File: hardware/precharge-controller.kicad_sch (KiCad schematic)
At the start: 0 parts

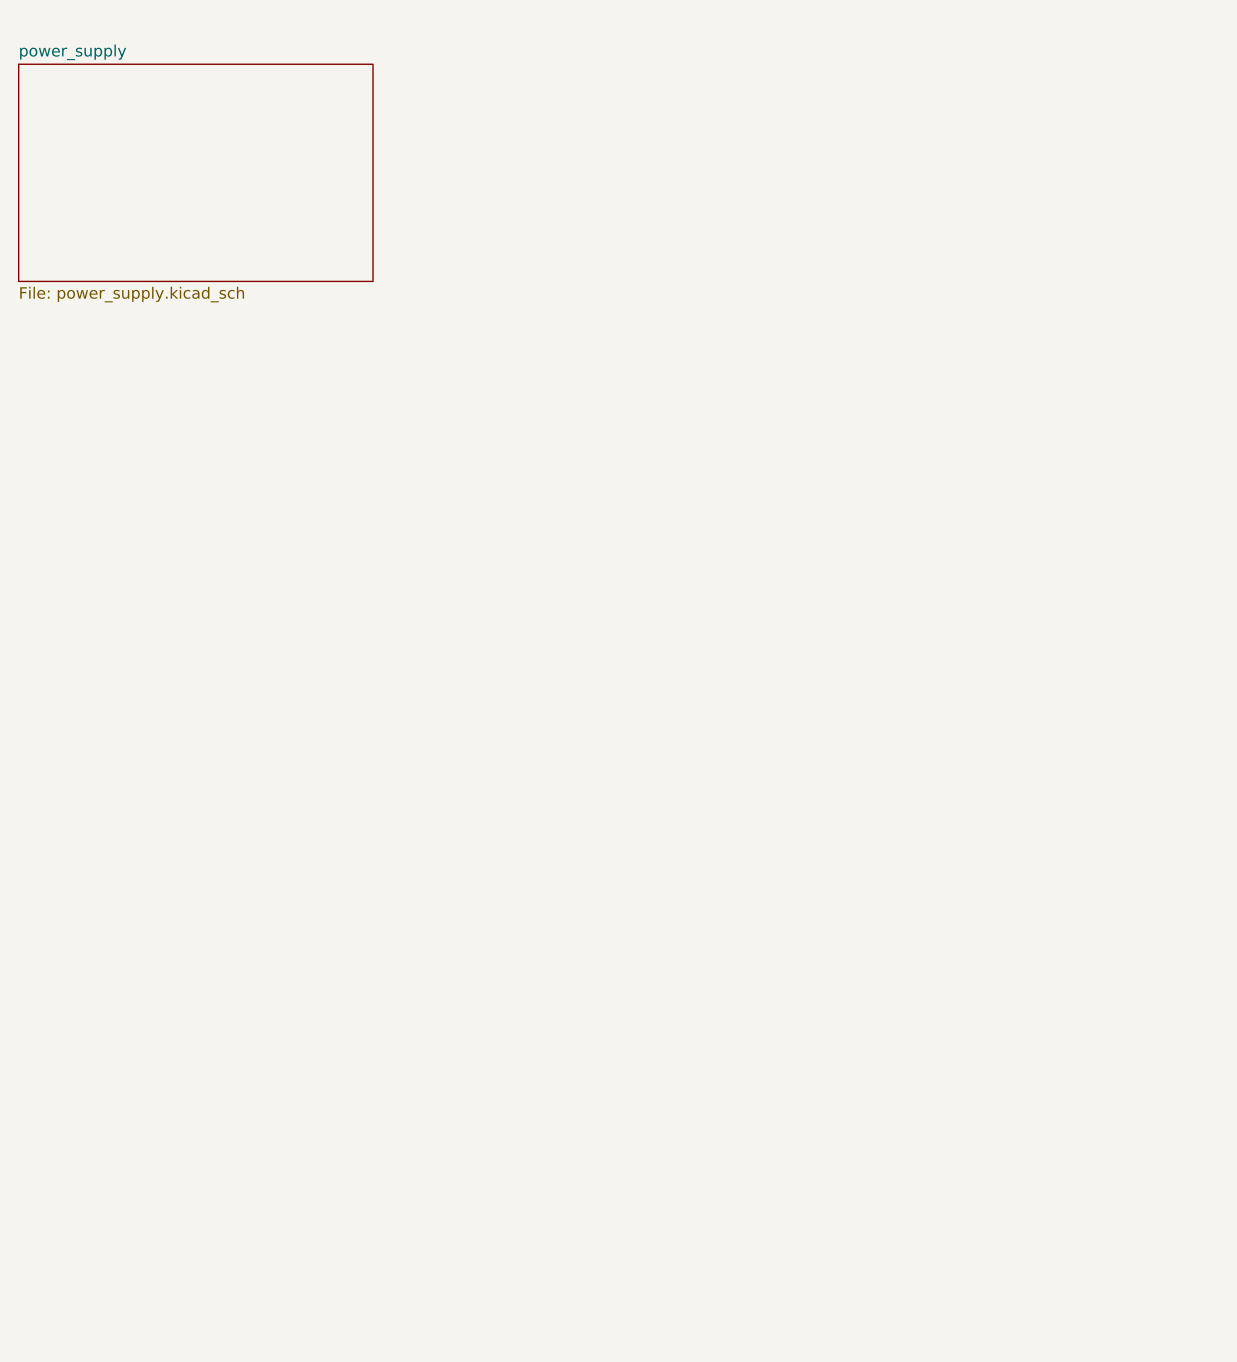
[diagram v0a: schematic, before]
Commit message: complete hierarchial sheet organization; start hv_sense schematic; start lv_logic schematic; refactor hierarchial sheets
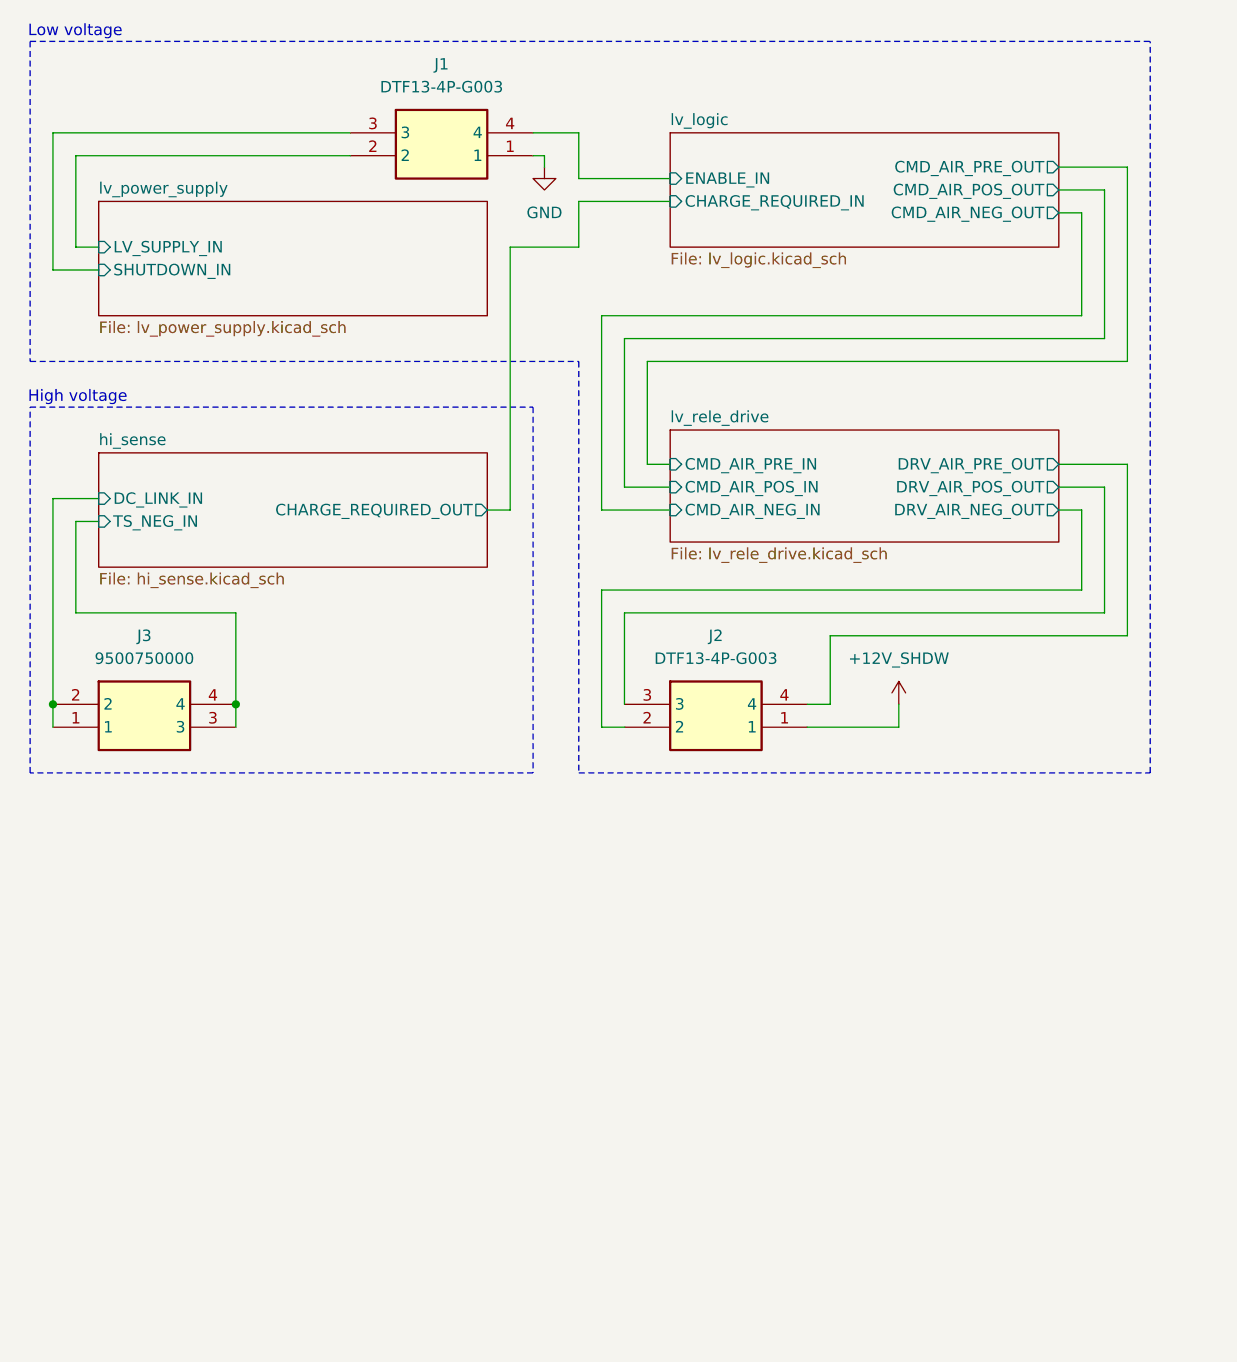
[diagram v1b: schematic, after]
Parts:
- added J1: DTF13-4P-G003, Library_Loader:DTF134PG003, symbol Libary_Loader:DTF13-4P-G003
- added J2: DTF13-4P-G003, DTF134PG003, symbol Libary_Loader:DTF13-4P-G003
- added J3: 9500750000, 9500750000, symbol Libary_Loader:9500750000
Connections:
- new net +12V_SHDW: J2.1
- new net GND: J1.1
- new net hi_sense/DC_LINK_IN: J3.1, J3.2
- new net hi_sense/TS_NEG_IN: J3.3, J3.4
- new net lv_logic/ENABLE_IN: J1.4
- new net lv_power_supply/LV_SUPPLY_IN: J1.2
- new net lv_power_supply/SHUTDOWN_IN: J1.3
- new net lv_rele_drive/DRV_AIR_NEG_OUT: J2.2
- new net lv_rele_drive/DRV_AIR_POS_OUT: J2.3
- new net lv_rele_drive/DRV_AIR_PRE_OUT: J2.4
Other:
- sheet power_supply renamed lv_power_supply
- added sheet hi_sense (hi_sense.kicad_sch)
- added sheet lv_logic (lv_logic.kicad_sch)
- added sheet lv_rele_drive (lv_rele_drive.kicad_sch)
- sheet lv_power_supply: file power_supply.kicad_sch -> lv_power_supply.kicad_sch
- sheet lv_power_supply ports: added LV_SUPPLY_IN, SHUTDOWN_IN; removed none
- note added: "High voltage"
- note added: "Low voltage"

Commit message: add enable timer sizing in logic block
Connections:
- net GND: no longer J1.1
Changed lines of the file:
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@@
-	(wire
-		(pts
-			(xy 81.28 38.1) (xy 82.55 38.1)
-		)
-		(stroke
-			(width 0)
-			(type default)
-		)
-	)
 	(wire
 		(pts

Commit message: create hv_power hierarchical sheet; rename hi_sense ad hv_sense to meet project standards
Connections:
- net GND: now also J1.1
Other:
- sheet hi_sense renamed hv_sense
- added sheet hv_power (hv_power.kicad_sch)
- sheet hv_sense: file hi_sense.kicad_sch -> hv_sense.kicad_sch
- note added: "On PCB"
- note added: "Outside PCB"
- moved on the sheet: J1, J2, J3

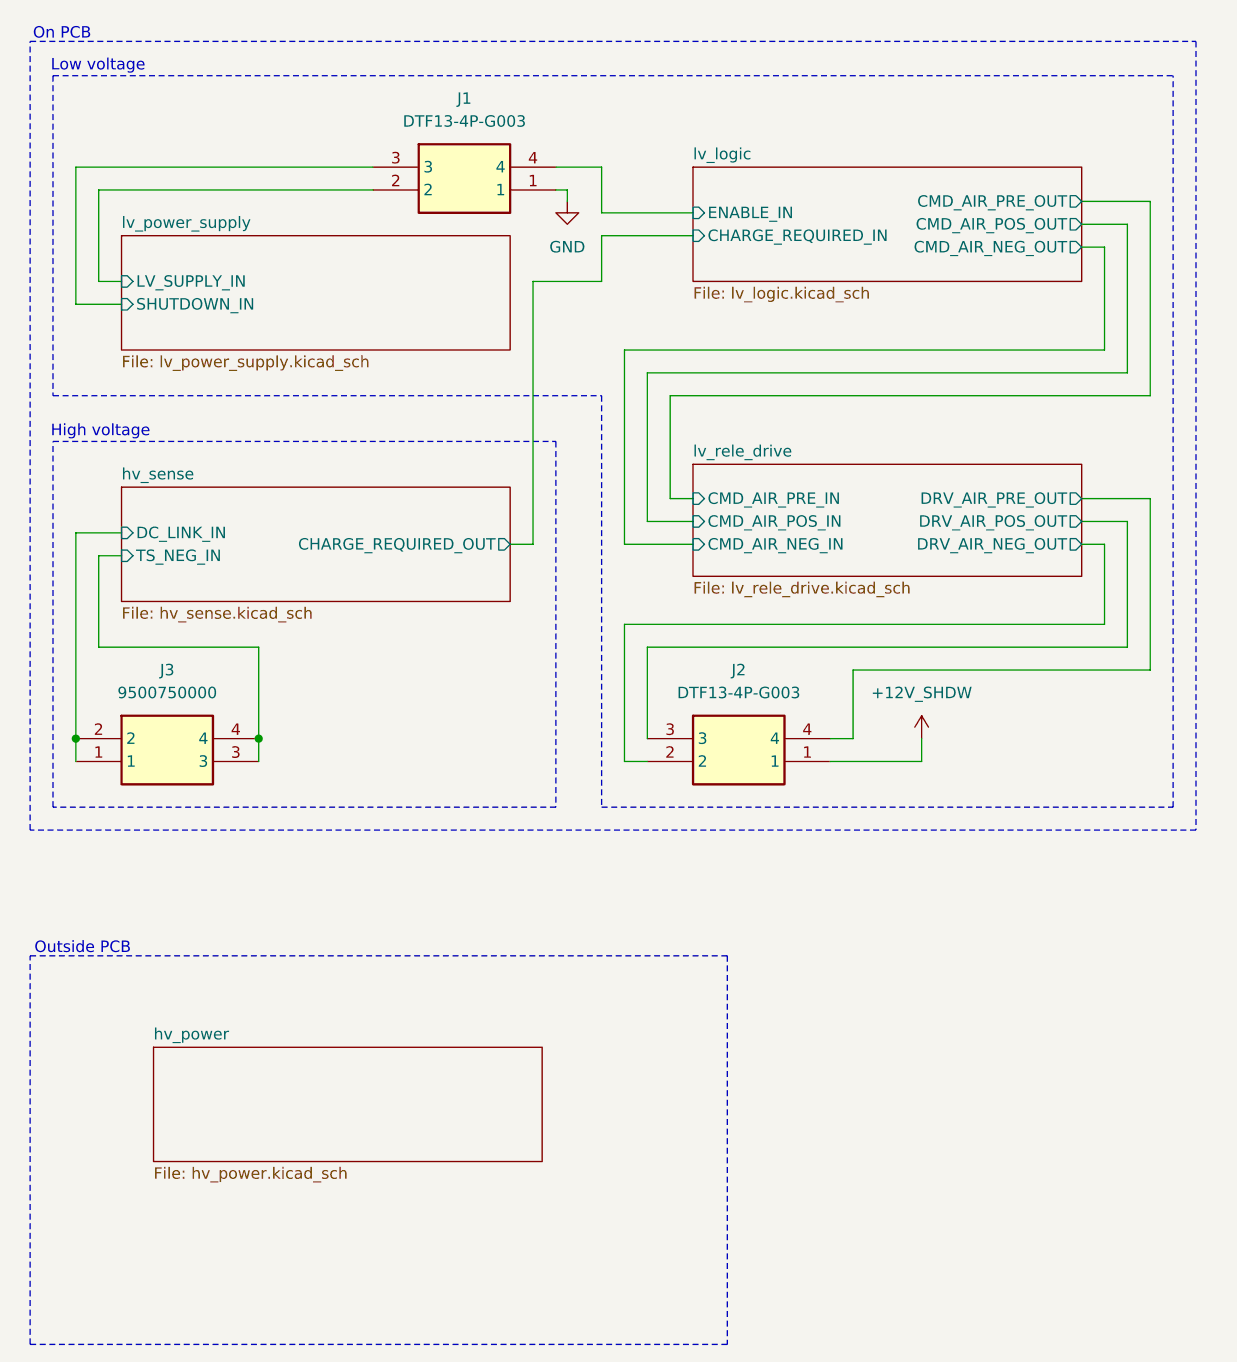
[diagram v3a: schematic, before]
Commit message: add traction system positive input to hv sense block with new dedicated connector
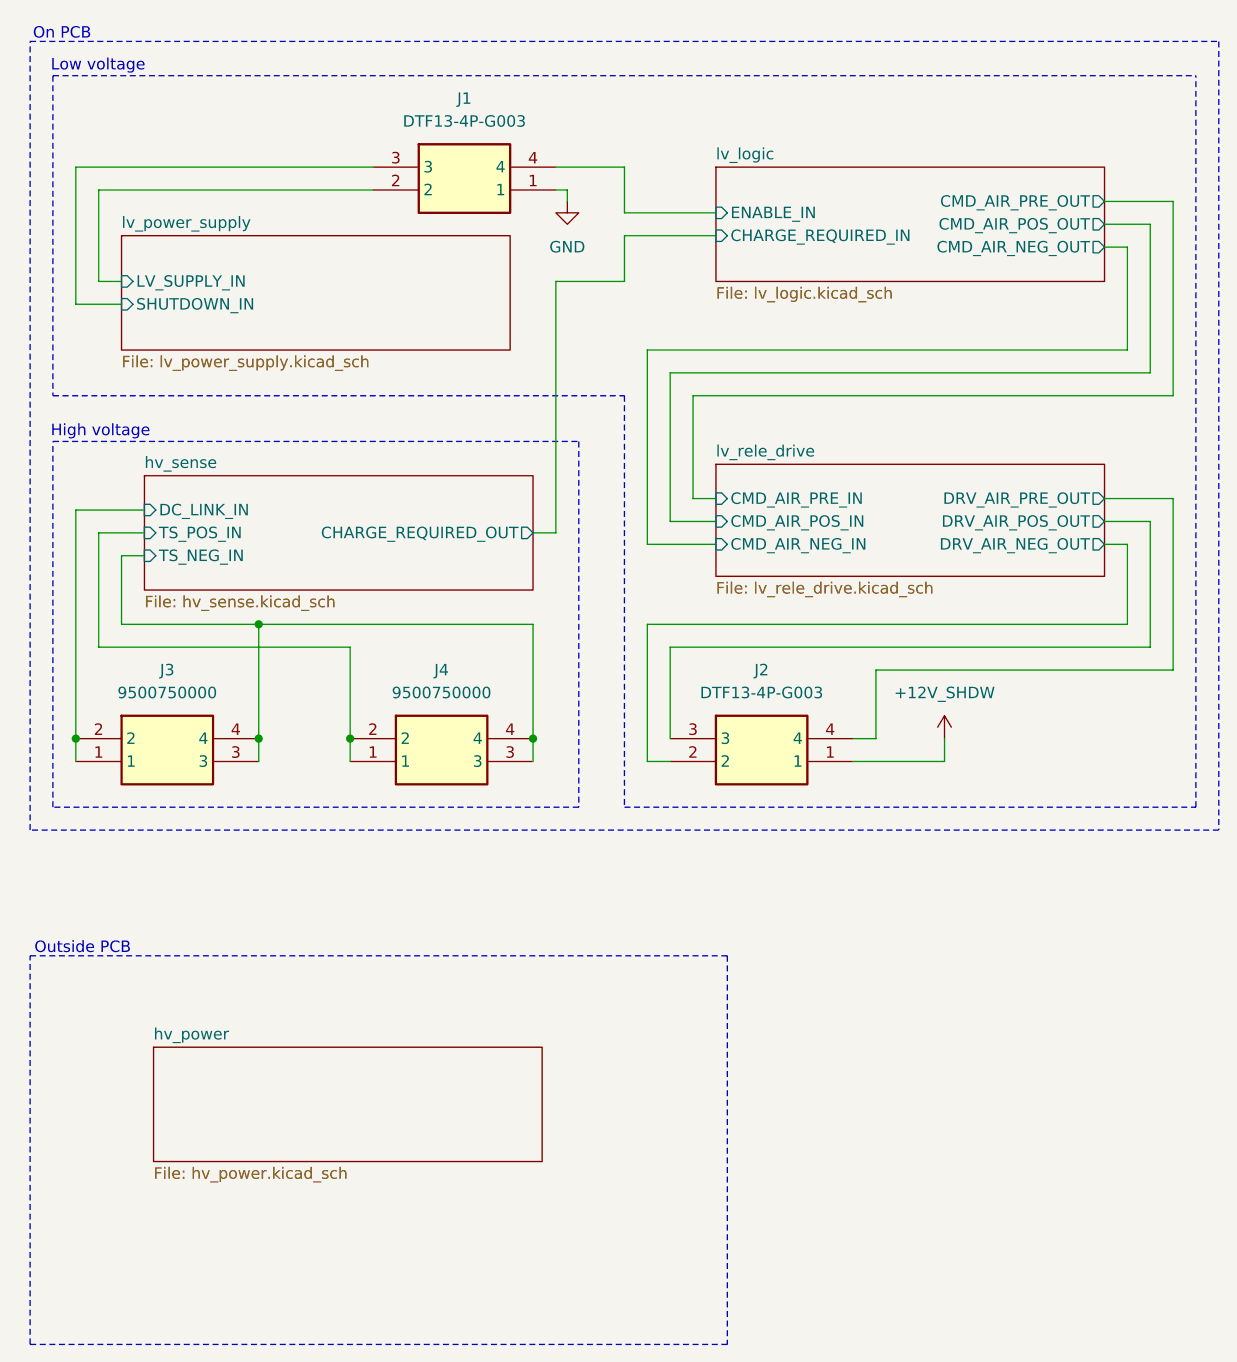
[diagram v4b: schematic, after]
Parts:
- added J4: 9500750000, 9500750000, symbol Libary_Loader:9500750000
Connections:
- net hv_sense/TS_NEG_IN: now also J4.3, J4.4
- new net hv_sense/TS_POS_IN: J4.1, J4.2
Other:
- sheet hv_sense ports: added TS_POS_IN; removed none
- moved on the sheet: J2

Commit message: refactor project layout merging high and low voltage in the same pcb
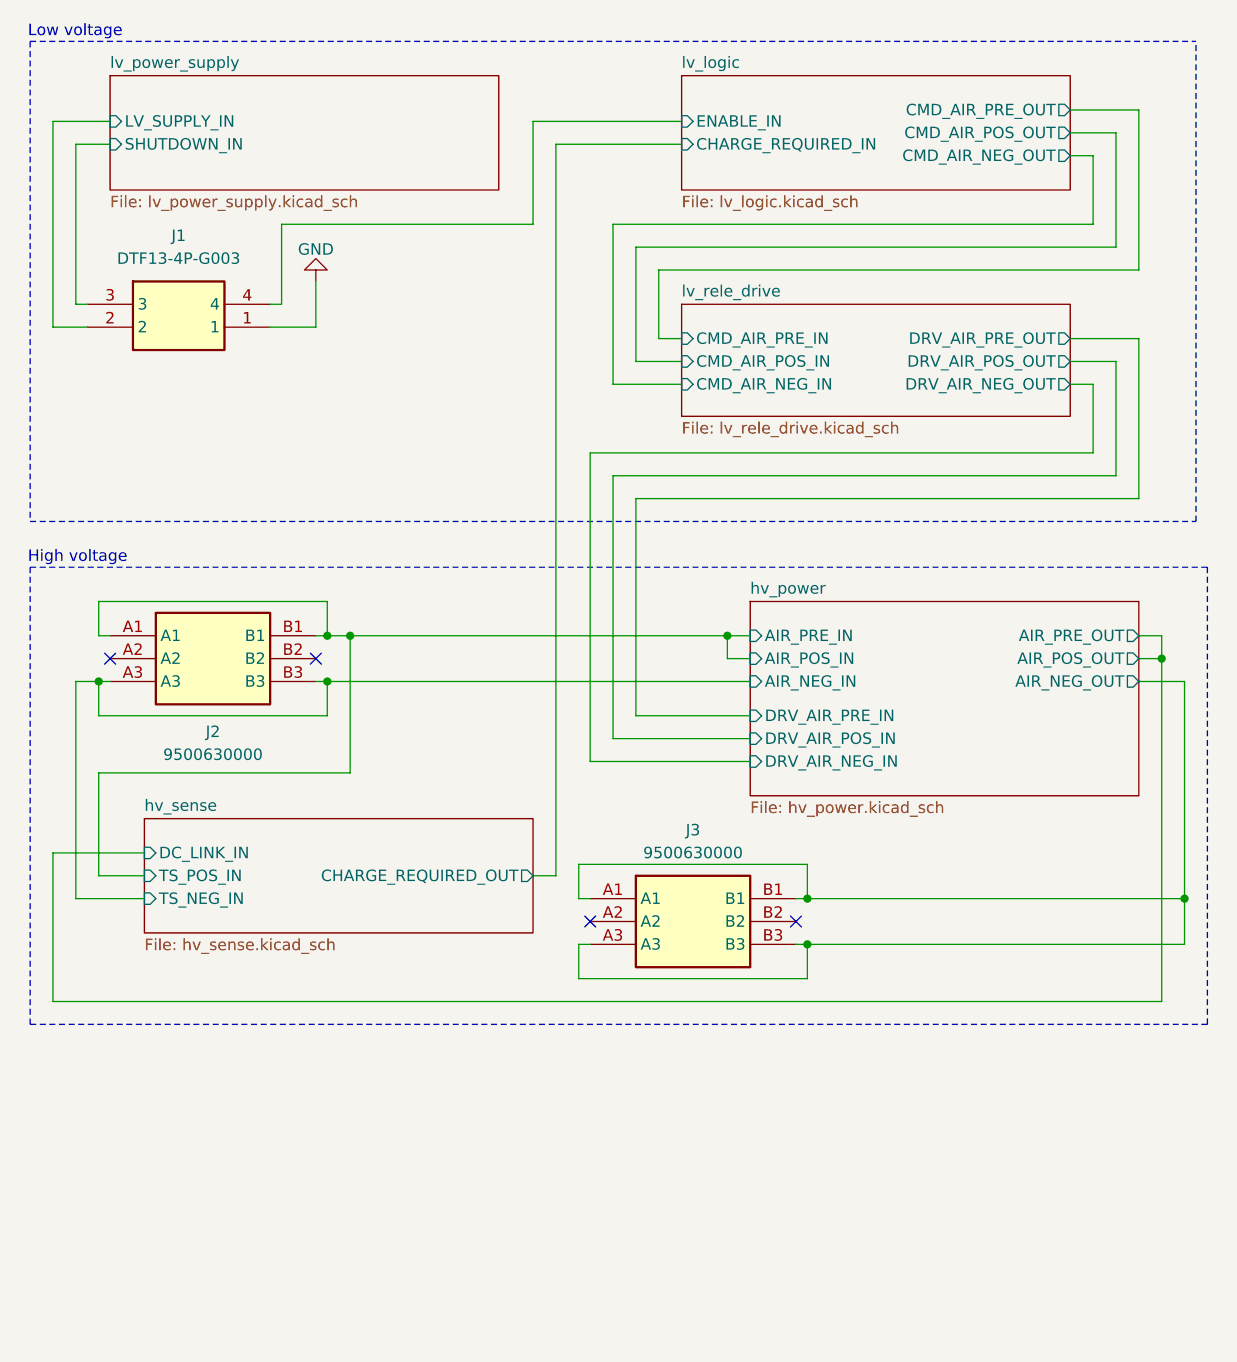
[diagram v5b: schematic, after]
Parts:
- removed J2: DTF13-4P-G003, DTF134PG003, symbol Libary_Loader:DTF13-4P-G003
- removed J3, J4: 9500750000, 9500750000, symbol Libary_Loader:9500750000
- added J2, J3: 9500630000, 9500630000, symbol Libary_Loader:9500630000
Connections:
- new net hv_power/AIR_NEG_IN: J2.A3, J2.B3
- new net hv_power/AIR_NEG_OUT: J3.A1, J3.A3, J3.B1, J3.B3
- new net hv_power/AIR_POS_IN: J2.A1, J2.B1
- no-connect marks 0 -> 4
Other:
- sheet hv_power ports: added AIR_NEG_IN, AIR_NEG_OUT, AIR_POS_IN, AIR_POS_OUT, AIR_PRE_IN, AIR_PRE_OUT, DRV_AIR_NEG_IN, DRV_AIR_POS_IN, DRV_AIR_PRE_IN; removed none
- note removed: "On PCB"
- note removed: "Outside PCB"
- moved on the sheet: J1

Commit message: refactor lv_rele_drive to lv_relay_drive
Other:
- sheet lv_rele_drive renamed lv_relay_drive
- sheet lv_relay_drive: file lv_rele_drive.kicad_sch -> lv_relay_drive.kicad_sch
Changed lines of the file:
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@@
 			(color 0 0 0 0)
 		)
-		(property "Sheetname" "lv_rele_drive"
+		(property "Sheetname" "lv_relay_drive"
 			(at 97.79 53.8984 0)
 			(show_name no)
@@
 			)
 		)
-		(property "Sheetfile" "lv_rele_drive.kicad_sch"
+		(property "Sheetfile" "lv_relay_drive.kicad_sch"
 			(at 97.79 67.6406 0)
 			(show_name no)

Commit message: start power supply and logic sizing
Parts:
- J2, J3: footprint 9500630000 -> Library_Loader:9500630000
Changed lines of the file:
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@@
 			)
 		)
-		(property "Footprint" "9500630000"
+		(property "Footprint" "Library_Loader:9500630000"
 			(at 106.68 215.57 0)
 			(hide yes)
@@
 			)
 		)
-		(property "Footprint" "9500630000"
+		(property "Footprint" "Library_Loader:9500630000"
 			(at 53.34 186.36 0)
 			(hide yes)
